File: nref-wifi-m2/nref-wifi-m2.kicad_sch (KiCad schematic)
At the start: 36 parts, among them J1 Bus_M.2_Socket_E, J2 Conn_01x20, U1 TPS62A04ABDRL, X1 ECS-327MVATX-2-CN-TR3

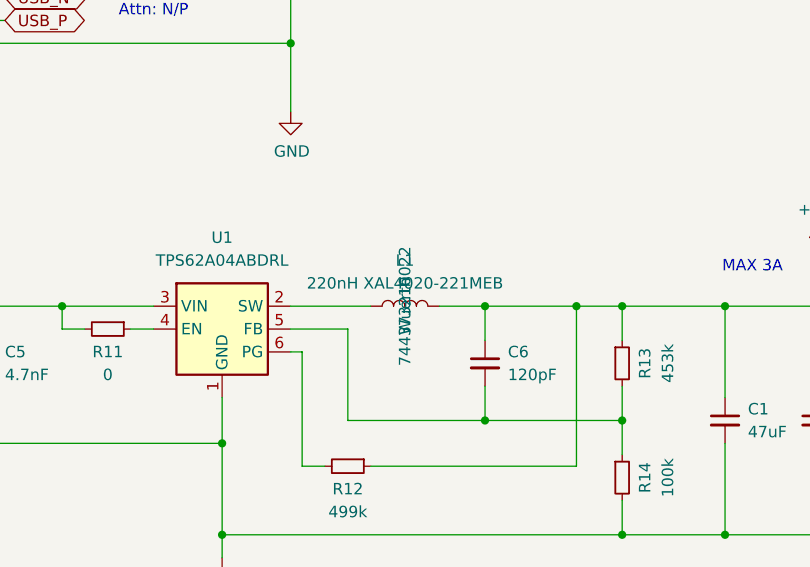
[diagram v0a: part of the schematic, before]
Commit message: wifi/bt board prod updates
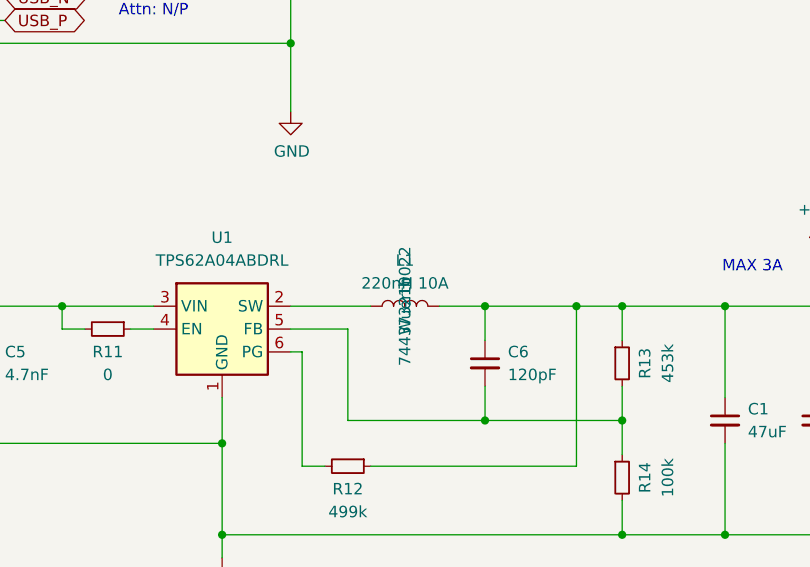
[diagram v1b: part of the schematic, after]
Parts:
- C1, C2: LCSC (none) -> C84494
- C4: LCSC (none) -> C39232; Manufacturer Murata -> Samsung; Manufacturer_No GRM32EC72A106KE05L -> CL32B106KAJNNNE
- C5: LCSC (none) -> C85980
- C6: LCSC (none) -> C18438
- C7: LCSC (none) -> C77058
- D1, D2: LCSC (none) -> C5875723
- H1: LCSC (none) -> C22431324
- J1: LCSC (none) -> C5163551
- J2: LCSC (none) -> C596730
- L1: value 220nH XAL4020-221MEB -> 220nH 10A; footprint Inductor_SMD:L_Coilcraft_XAL4020-XXX -> EasyEDA:IND-SMD_L3.0-W3.0_FTC303020D; LCSC (none) -> C5832405; Manufacturer Coilcraft -> cjiang; Manufacturer_No XAL4020-221MEB -> FTC303018DR22MBCA
- R1, R5, R6, R7, R8, R9: LCSC (none) -> C25804; Manufacturer Yageo -> UNI-ROYAL; Manufacturer_No RC0603FR-0710KL -> 0603WAF1002T5E
- R10, R11, R2: LCSC (none) -> C21189; Manufacturer Yageo -> UNI-ROYAL; Manufacturer_No RC0603JR-070RL -> 0603WAF0000T5E
- R12: LCSC (none) -> C26751; Manufacturer Yageo -> UNI-ROYAL; Manufacturer_No RC0603FR-07499KL -> 0603WAF4993T5E
- R13: LCSC (none) -> C25818; Manufacturer Vishay Dale -> UNI-ROYAL; Manufacturer_No CRCW0603453KFKEA -> 0603WAF4533T5E
- R14: LCSC (none) -> C25803; Manufacturer Yageo -> UNI-ROYAL; Manufacturer_No RC0603FR-07100KL -> 0603WAF1003T5E
- R3, R4: LCSC (none) -> C22975; Manufacturer Yageo -> UNI-ROYAL; Manufacturer_No RC0603FR-072KL -> 0603WAF2001T5E
- U1: LCSC (none) -> C41447443
- X1: LCSC (none) -> C2901603; Manufacturer ECS -> SCTF; Manufacturer_No ECS-327MVATX-2-CN-TR3 -> SX2M32.768KM20F30TNN

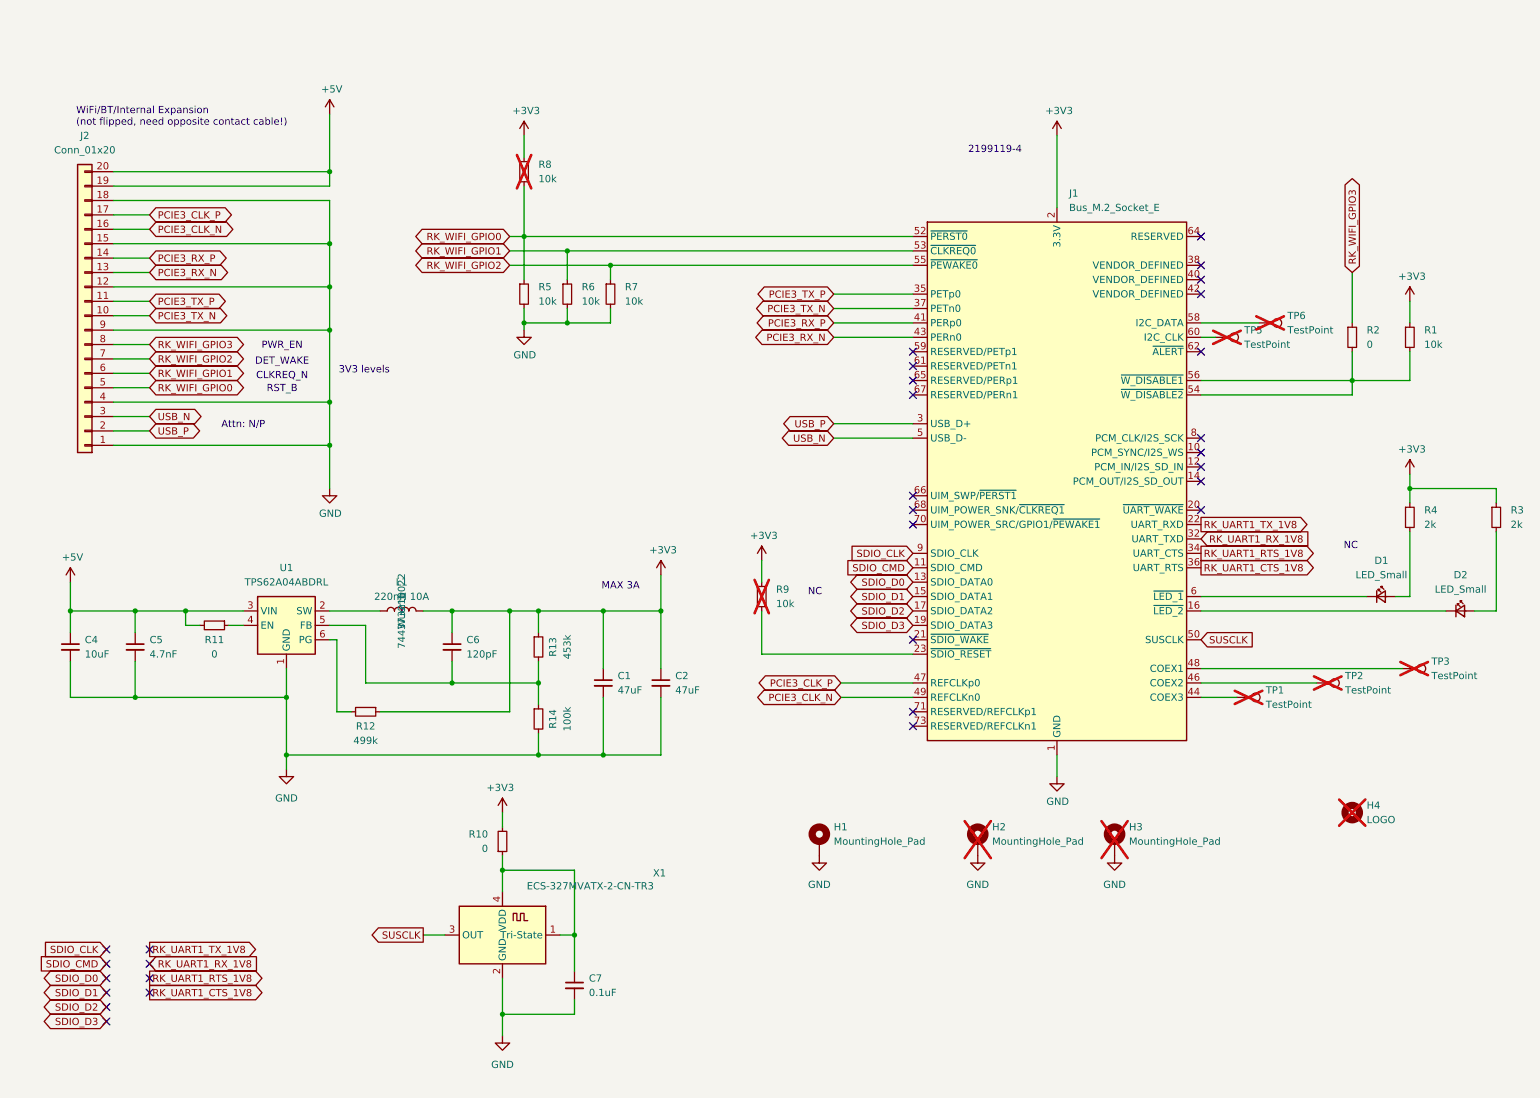
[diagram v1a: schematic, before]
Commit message: small schematic cleanups for book
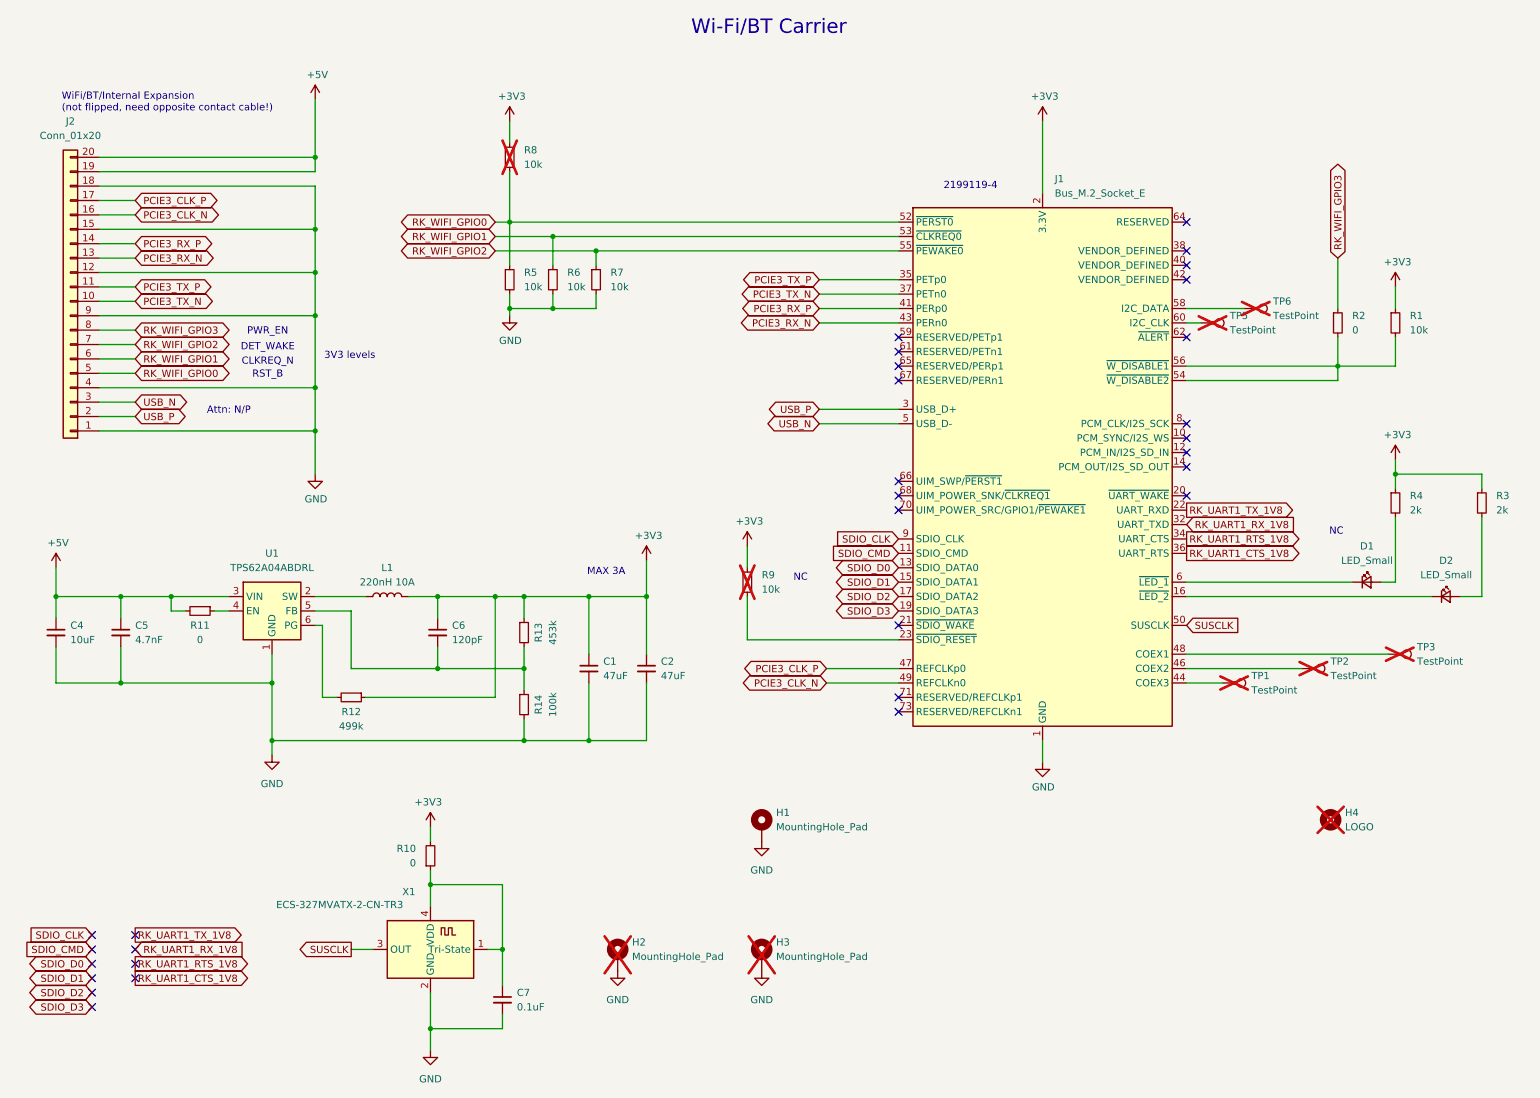
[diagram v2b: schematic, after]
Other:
- note added: "Wi-Fi/BT Carrier"
- company: (none) -> MNT Research GmbH, Copyright 2026
- title: (none) -> MNT Reform Next Wi-Fi/BT Carrier
- moved on the sheet: C1, C2, C4, C5, C6, C7, D1, D2, H1, H2, H3, H4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
